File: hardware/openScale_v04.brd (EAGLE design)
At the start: 55.9 x 47 mm, 74 parts, among them J1 3.3V, J2 UL, J3 UR, J4 LL, J5 LR, Q1 200mA/50V, Q2 200mA/50V, Q3 MMBT4403, Q4 MOSFET-NCHANNEL2N7002PW, U1 HX711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

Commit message: Updated board file
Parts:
- moved JP5 2.13 mm to (27.9, 43.2)
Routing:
- net GND: track 298.1 -> 307.0 mm, vias 36 -> 39
- net 5V: track 161.6 -> 169.0 mm
- net D11: track 17.0 -> 15.7 mm, vias 1 -> 0
- net RST: track 57.0 -> 58.1 mm
- net D13: track 42.8 -> 43.6 mm
- net D12: track 12.7 -> 12.2 mm, vias 1 -> 0

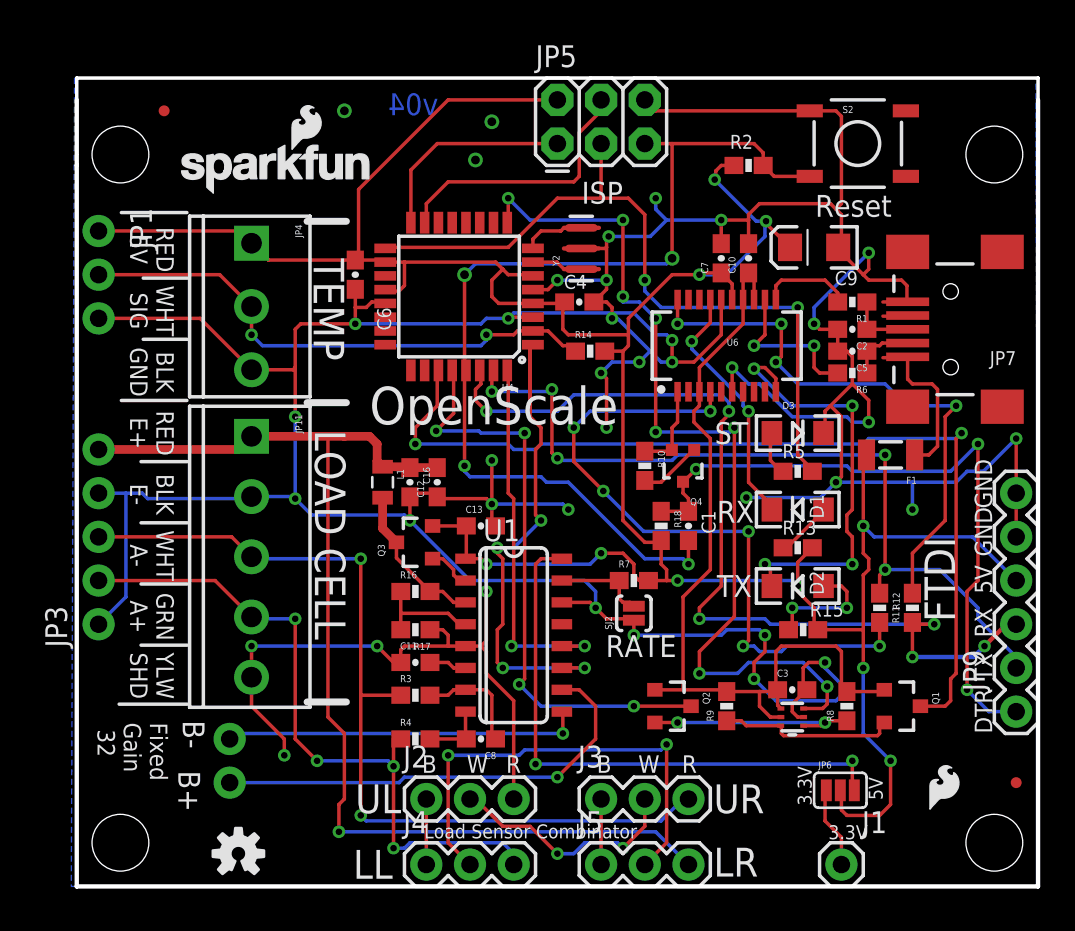
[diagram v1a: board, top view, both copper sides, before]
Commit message: Updated Board and Schematic files per QC checklist
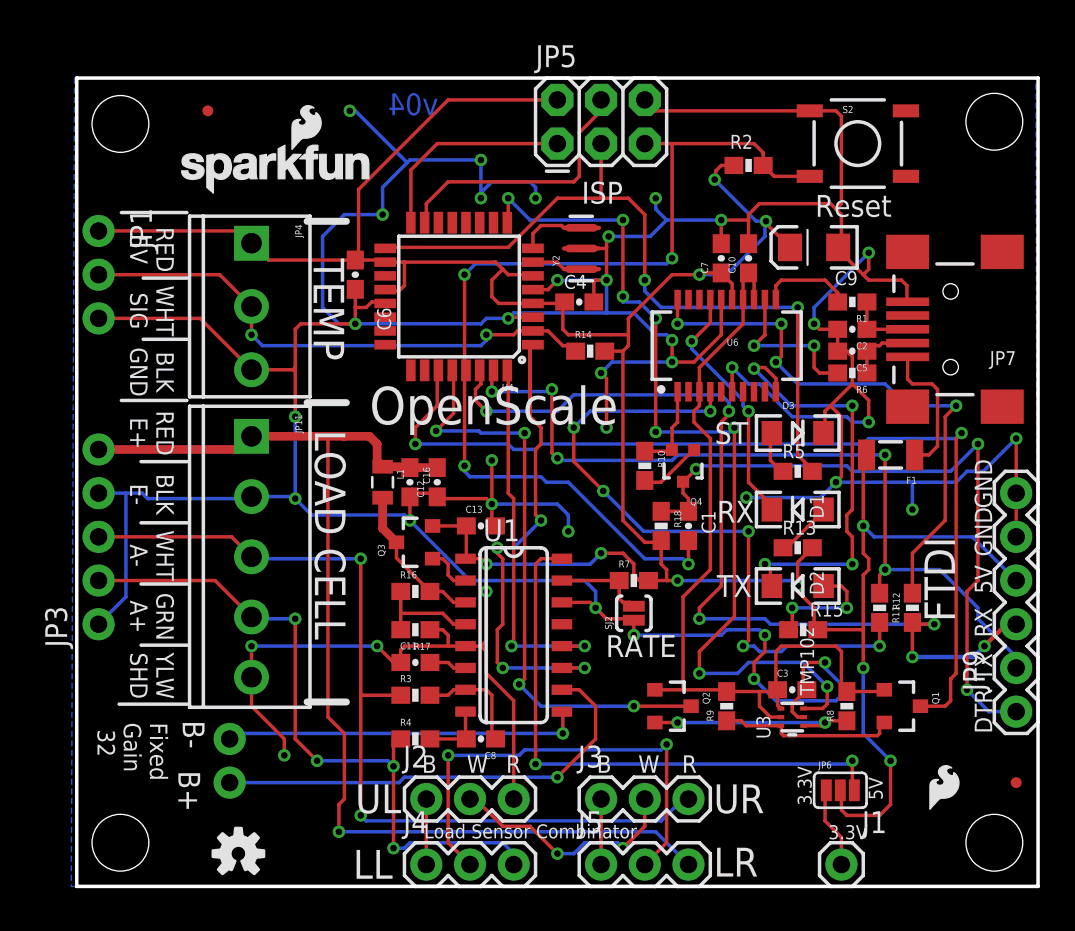
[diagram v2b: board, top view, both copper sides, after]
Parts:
- moved FID2 2.54 mm to (7.62, 45.1)
- moved STANDOFF1 1.91 mm to (53.3, 44.5)
- moved STANDOFF4 1.78 mm to (2.54, 44.3)
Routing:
- net GND: track 307.0 -> 334.7 mm
- net N$38: track 0.51 -> 0.00 mm
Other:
- outline, holes or cut-outs redrawn

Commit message: Updated yellow LED
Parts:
- D1: value YELLOW -> Yellow
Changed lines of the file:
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@@
 <setting verticaltext="up"/>
 </settings>
-<grid distance="0.0125" unitdist="inch" unit="inch" style="lines" multiple="1" display="yes" altdistance="0.005" altunitdist="inch" altunit="inch"/>
+<grid distance="0.05" unitdist="inch" unit="inch" style="lines" multiple="1" display="yes" altdistance="0.005" altunitdist="inch" altunit="inch"/>
 <layers>
 <layer number="1" name="Top" color="4" fill="1" visible="yes" active="yes"/>
@@
 <layer number="23" name="tOrigins" color="15" fill="1" visible="yes" active="yes"/>
 <layer number="24" name="bOrigins" color="15" fill="1" visible="yes" active="yes"/>
-<layer number="25" name="tNames" color="7" fill="1" visible="yes" active="yes"/>
-<layer number="26" name="bNames" color="7" fill="1" visible="yes" active="yes"/>
-<layer number="27" name="tValues" color="7" fill="1" visible="yes" active="yes"/>
-<layer number="28" name="bValues" color="7" fill="1" visible="yes" active="yes"/>
+<layer number="25" name="tNames" color="7" fill="1" visible="no" active="yes"/>
+<layer number="26" name="bNames" color="7" fill="1" visible="no" active="yes"/>
+<layer number="27" name="tValues" color="7" fill="1" visible="no" active="yes"/>
+<layer number="28" name="bValues" color="7" fill="1" visible="no" active="yes"/>
 <layer number="29" name="tStop" color="5" fill="1" visible="no" active="yes"/>
 <layer number="30" name="bStop" color="7" fill="6" visible="no" active="yes"/>
@@
 <layer number="43" name="vRestrict" color="2" fill="10" visible="no" active="yes"/>
 <layer number="44" name="Drills" color="7" fill="1" visible="no" active="yes"/>
-<layer number="45" name="Holes" color="7" fill="1" visible="no" active="yes"/>
+<layer number="45" name="Holes" color="7" fill="1" visible="yes" active="yes"/>
 <layer number="46" name="Milling" color="3" fill="1" visible="no" active="yes"/>
 <layer number="47" name="Measures" color="7" fill="1" visible="no" active="yes"/>
@@
 <layer number="49" name="Reference" color="7" fill="1" visible="no" active="yes"/>
 <layer number="50" name="dxf" color="7" fill="1" visible="no" active="no"/>
-<layer number="51" name="tDocu" color="6" fill="1" visible="no" active="yes"/>
+<layer number="51" name="tDocu" color="6" fill="1" visible="yes" active="yes"/>
 <layer number="52" name="bDocu" color="7" fill="1" visible="no" active="yes"/>
 <layer number="53" name="tGND_GNDA" color="7" fill="9" visible="no" active="no"/>
@@
 <attribute name="PROD_ID" value="CONN-08193" x="50.8" y="32.385" size="1.778" layer="27" rot="R180" display="off"/>
 </element>
-<element name="D1" library="SparkFun-LED" package="LED-1206" value="YELLOW" x="41.91" y="21.9075" smashed="yes" rot="R180">
+<element name="D1" library="SparkFun-LED" package="LED-1206" value="Yellow" x="41.91" y="21.9075" smashed="yes" rot="R180">
 <attribute name="NAME" x="42.6085" y="22.7965" size="0.8128" layer="25" font="vector" ratio="15" rot="R270"/>
-<attribute name="VALUE" value="YELLOW" x="40.8305" y="22.9235" size="0.8128" layer="27" font="vector" ratio="15" rot="R270"/>
-<attribute name="PROD_ID" value="DIO-00820" x="41.91" y="21.9075" size="1.778" layer="27" rot="R180" display="off"/>
+<attribute name="VALUE" value="Yellow" x="40.8305" y="22.9235" size="0.8128" layer="27" font="vector" ratio="15" rot="R270"/>
+<attribute name="PROD_ID" value="DIO-09909" x="41.91" y="21.9075" size="1.778" layer="27" rot="R180" display="off"/>
 </element>
 <element name="D2" library="SparkFun-LED" package="LED-1206" value="GREEN" x="41.91" y="17.4625" smashed="yes" rot="R180">

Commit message: Updated Board and Schemtic
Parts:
- added C14: 0.1uF, SparkFun-Capacitors:0603-CAP
- moved LOGO2 28.0 mm to (31.0, 19.7)
- moved LOGO4 24.2 mm to (36.6, 26.0)
- moved LOGO5 3.14 mm to (12.4, 2.67)
- moved JP1 1.27 mm to (1.27, 36.8), flipped to the bottom
- moved LOGO1 0.92 mm to (4.89, 40.7)
- moved R18 0.32 mm to (34.3, 21.0)
- moved JP4 0.23 mm to (10.2, 37.0)
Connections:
- removed net N$33: Q4.1, R10.2
- net 3.3V: now also Q4.1, R10.2
- net GND: now also C14.2
- net N$12: now also C14.1
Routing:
- net 3.3V: track 50.0 -> 54.7 mm
- net N$33: track 3.69 -> 0.00 mm
- net N$12: track 8.12 -> 10.3 mm
- net 5V: track 169.0 -> 167.5 mm
- net LV_SDA: track 10.3 -> 11.7 mm
- net TEMP_DAT: track 31.4 -> 30.1 mm
- net GND: track 334.7 -> 335.4 mm
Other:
- outline, holes or cut-outs redrawn
- board text added: "+"
- board text added: "-"
- board text added: "C"
- board text removed: "B"
- board text removed: "R"
- board text removed: "W"

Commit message: Updated silk on brd file
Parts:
- moved LOGO5 1.27 mm to (12.4, 3.94)
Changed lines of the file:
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@@
 <grid distance="0.05" unitdist="inch" unit="inch" style="lines" multiple="1" display="yes" altdistance="0.005" altunitdist="inch" altunit="inch"/>
 <layers>
-<layer number="1" name="Top" color="4" fill="1" visible="yes" active="yes"/>
+<layer number="1" name="Top" color="4" fill="1" visible="no" active="yes"/>
 <layer number="2" name="Route2" color="1" fill="3" visible="no" active="no"/>
 <layer number="3" name="Route3" color="4" fill="3" visible="no" active="no"/>
@@
 </element>
 <element name="LOGO1" library="SparkFun-Aesthetics" package="SFE_LOGO_NAME_FLAME_.1" value="SFE_LOGO_NAME_FLAME.1_INCH" x="4.8895" y="40.7035"/>
-<element name="LOGO5" library="SparkFun-Aesthetics" package="OSHW-LOGO-S" value="OSHW-LOGOS" x="12.446" y="2.667"/>
+<element name="LOGO5" library="SparkFun-Aesthetics" package="OSHW-LOGO-S" value="OSHW-LOGOS" x="12.446" y="3.937"/>
 <element name="C14" library="SparkFun-Capacitors" package="0603-CAP" value="0.1uF" x="48.768" y="23.114" rot="R180">
 <attribute name="PROD_ID" value="CAP-00810" x="48.768" y="23.114" size="1.778" layer="27" font="vector" ratio="15" rot="R180" display="off"/>
@@
 <wire x1="32.0675" y1="32.0675" x2="32.0675" y2="33.02" width="0.2032" layer="1"/>
 <wire x1="32.0675" y1="33.02" x2="34.6075" y2="35.56" width="0.2032" layer="1"/>
-<wire x1="20.685" y1="20.9525" x2="22.6425" y2="20.9525" width="0.2032" layer="1"/>
+<wire x1="20.685" y1="20.9525" x2="22.6425" y2="20.9525" width="0.508" layer="1"/>
 <wire x1="22.6425" y1="20.9525" x2="22.645" y2="20.955" width="0.2032" layer="1"/>
-<wire x1="22.645" y1="20.955" x2="22.645" y2="19.095" width="0.2032" layer="1"/>
+<wire x1="22.645" y1="20.955" x2="22.645" y2="19.095" width="0.508" layer="1"/>
 <wire x1="22.645" y1="19.095" x2="22.6" y2="19.05" width="0.2032" layer="1"/>
 <wire x1="33.02" y1="17.78" x2="33.235" y2="17.78" width="0.2032" layer="1"/>

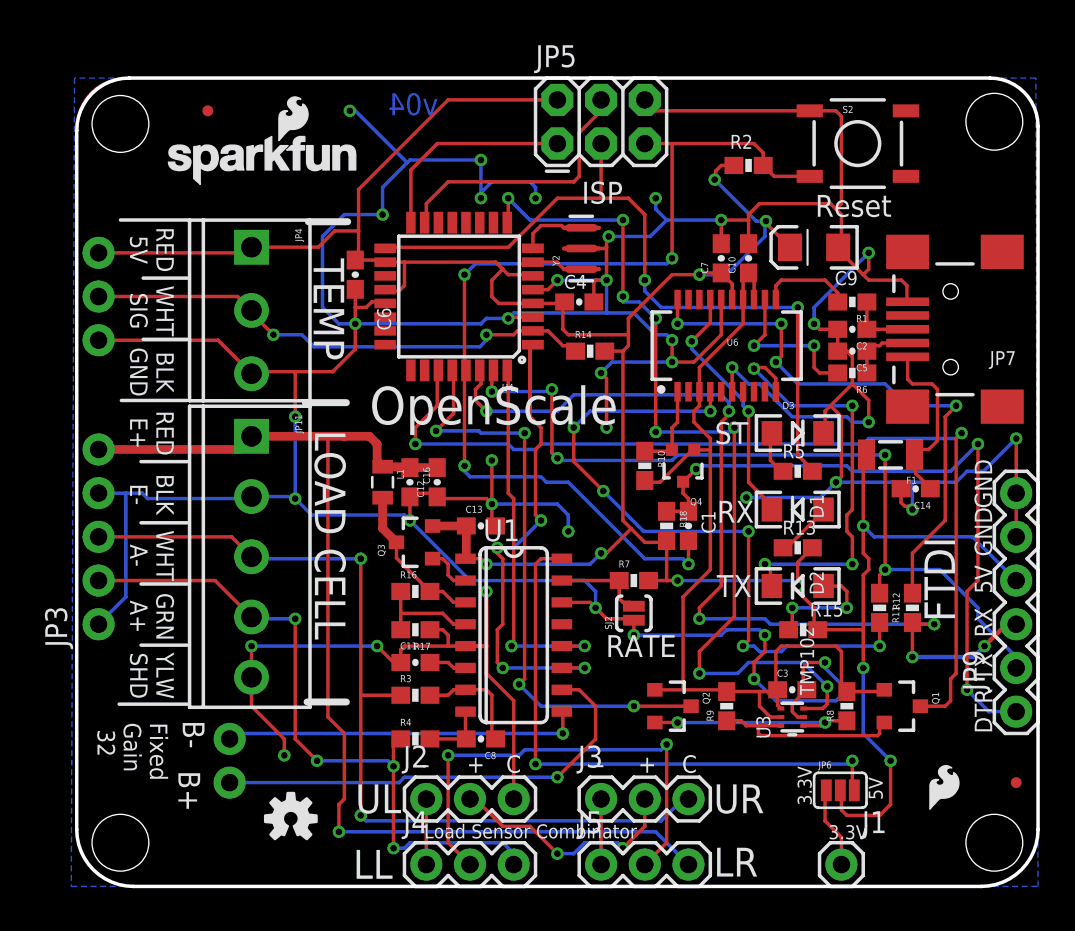
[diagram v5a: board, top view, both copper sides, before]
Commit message: Updated BRD and SCH file per Engineering Design Review
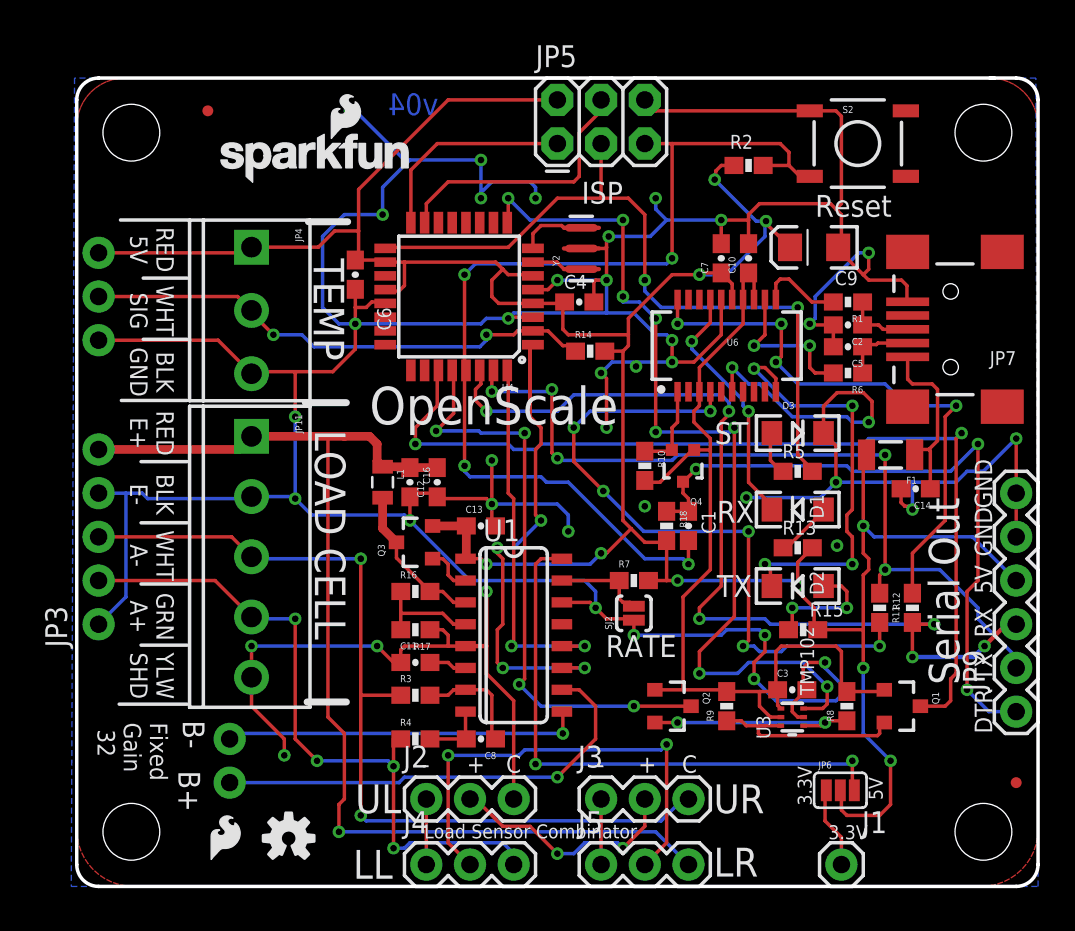
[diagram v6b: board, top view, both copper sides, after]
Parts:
- moved LOGO3 41.9 mm to (7.49, 1.21)
- moved LOGO1 3.05 mm to (7.94, 40.8)
- moved LOGO5 1.15 mm to (12.3, 2.79)
- moved STANDOFF1 0.90 mm to (52.7, 43.8)
- moved STANDOFF2 0.90 mm to (52.7, 3.17)
- moved STANDOFF3 0.90 mm to (3.17, 3.17)
- moved STANDOFF4 0.81 mm to (3.17, 43.8)
- moved C2 0.36 mm to (44.8, 32.6)
- moved C5 0.36 mm to (44.8, 31.4)
- moved R1 0.25 mm to (44.8, 34.0)
- moved R6 0.25 mm to (44.8, 29.8)
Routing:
- net GND: track 335.4 -> 331.5 mm, vias 39 -> 42
- net RST: track 58.1 -> 59.6 mm
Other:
- outline, holes or cut-outs redrawn
- board text added: "Serial Out"
- board text removed: "FTDI"

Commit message: Updated Brd and Sch files per QC review.
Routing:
- net GND: vias 42 -> 43
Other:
- board text added: "v10"
- board text removed: "v04"
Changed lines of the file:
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@@
 <setting verticaltext="up"/>
 </settings>
-<grid distance="0.01" unitdist="inch" unit="inch" style="lines" multiple="1" display="yes" altdistance="0.005" altunitdist="inch" altunit="inch"/>
+<grid distance="0.05" unitdist="inch" unit="inch" style="lines" multiple="1" display="yes" altdistance="0.005" altunitdist="inch" altunit="inch"/>
 <layers>
 <layer number="1" name="Top" color="4" fill="1" visible="yes" active="yes"/>
@@
 <layer number="45" name="Holes" color="7" fill="1" visible="yes" active="yes"/>
 <layer number="46" name="Milling" color="3" fill="1" visible="no" active="yes"/>
-<layer number="47" name="Measures" color="7" fill="1" visible="yes" active="yes"/>
+<layer number="47" name="Measures" color="7" fill="1" visible="no" active="yes"/>
 <layer number="48" name="Document" color="7" fill="1" visible="no" active="yes"/>
 <layer number="49" name="Reference" color="7" fill="1" visible="no" active="yes"/>
@@
 <text x="50.9905" y="21.971" size="1.016" layer="22" font="vector" ratio="15" rot="MR90">BLK</text>
 <text x="52.0065" y="11.4935" size="1.016" layer="22" font="vector" ratio="15" rot="MR270">GRN</text>
-<text x="21.0185" y="44.831" size="1.27" layer="16" font="vector" ratio="15" rot="MR0">v04</text>
+<text x="12.7635" y="44.45" size="1.27" layer="16" font="vector" ratio="15" rot="MR0">v10</text>
 <text x="4.372" y="22.787" size="1.016" layer="21" font="vector" ratio="15" rot="SR270" align="center">BLK
 E-</text>
@@
 <text x="24.9555" y="6.604" size="1.016" layer="21" font="vector" ratio="15">C</text>
 <text x="16.51" y="-11.43" size="1.778" layer="51" font="vector">Revision By: Mary West</text>
-<text x="49.53" y="22.606" size="1.778" layer="21" font="vector" ratio="15" rot="R270">Serial Out</text>
+<text x="50.292" y="21.844" size="1.27" layer="21" font="vector" ratio="15" rot="R270">Serial Out</text>
 <text x="68.58" y="21.9075" size="1.778" layer="47" font="vector">All units in Inches</text>
 <text x="41.91" y="6.985" size="0.8128" layer="21" font="vector" ratio="15" rot="R270">3.3V</text>
@@
 <wire x1="1.27" y1="31.75" x2="8.2146" y2="31.75" width="0.2032" layer="1"/>
 <wire x1="8.2146" y1="31.75" x2="10.16" y2="29.8046" width="0.2032" layer="1"/>
-<polygon width="0.2032" layer="1" isolate="0.3048">
-<vertex x="2.794" y="46.99"/>
-<vertex x="53.086" y="46.99" curve="-90"/>
-<vertex x="55.88" y="44.196"/>
-<vertex x="55.88" y="3.302" curve="-90"/>
-<vertex x="52.578" y="0"/>
-<vertex x="3.302" y="0" curve="-90"/>
-<vertex x="0" y="3.302"/>
-<vertex x="0" y="44.196" curve="-90"/>
-</polygon>
 <wire x1="23.8125" y1="12.3825" x2="23.8125" y2="13.97" width="0.254" layer="1"/>
 <wire x1="23.8125" y1="13.97" x2="23.8125" y2="17.145" width="0.254" layer="1"/>
@@
 <via x="33.02" y="22.098" extent="1-16" drill="0.381"/>
 <via x="44.196" y="19.812" extent="1-16" drill="0.381"/>
+<via x="38.989" y="10.541" extent="1-16" drill="0.381"/>
+<polygon width="0.2032" layer="1" isolate="0.3048">
+<vertex x="0" y="46.99"/>
+<vertex x="55.88" y="46.99"/>
+<vertex x="55.88" y="0"/>
+<vertex x="0" y="0"/>
+</polygon>
 </signal>
 <signal name="RST">
@@
 <wire x1="39.6875" y1="11.3275" x2="40.64" y2="11.3275" width="0.2032" layer="1"/>
 <wire x1="40.64" y1="11.3275" x2="40.7425" y2="11.43" width="0.2032" layer="1"/>
-<wire x1="40.7425" y1="11.43" x2="40.7425" y2="10.5325" width="0.2032" layer="1"/>
-<wire x1="40.7425" y1="10.5325" x2="40.9325" y2="10.3425" width="0.2032" layer="1"/>
 <wire x1="40.9325" y1="9.8425" x2="40.3225" y2="9.8425" width="0.2032" layer="1"/>
-<wire x1="40.3225" y1="9.8425" x2="39.6875" y2="10.4775" width="0.2032" layer="1"/>
+<wire x1="40.3225" y1="9.8425" x2="40.0685" y2="10.0965" width="0.2032" layer="1"/>
+<wire x1="40.0685" y1="10.0965" x2="39.6875" y2="10.4775" width="0.2032" layer="1"/>
 <wire x1="39.6875" y1="10.4775" x2="39.6875" y2="11.3275" width="0.2032" layer="1"/>
 <wire x1="40.64" y1="11.5325" x2="40.7425" y2="11.43" width="0.2032" layer="1"/>
@@
 <wire x1="33.909" y1="23.495" x2="33.1225" y2="23.495" width="0.2032" layer="1"/>
 <wire x1="33.1225" y1="23.495" x2="33.02" y2="23.5975" width="0.2032" layer="1"/>
+<wire x1="40.9325" y1="10.3425" x2="40.3145" y2="10.3425" width="0.2032" layer="1"/>
+<wire x1="40.3145" y1="10.3425" x2="40.0685" y2="10.0965" width="0.2032" layer="1"/>
 </signal>
 <signal name="RXLED">
